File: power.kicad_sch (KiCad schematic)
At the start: 23 parts, among them J1 Power, Q1 SI2301CDS-T1-GE3, U1 TMA-1212D, U2 TPS54302

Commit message: add placement notes into the schematic
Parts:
- U1: Placement (none) -> Separate from analog signal path. Digital ground side.
- U2: Placement (none) -> Follow TPS54302 datasheet layout rules. Digital ground. Kee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
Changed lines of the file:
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@@
+			)
+		)
+		(property "Placement" "Follow TPS54302 datasheet layout rules. Digital ground. Keep switching noise away from analog section."
+			(at 161.29 52.07 0)
+			(effects
+				(font
+					(size 1.27 1.27)
+				)
+				(hide yes)
 			)
 		)
@@
 			(at 60.96 130.81 0)
 			(effects
+				(font
+					(size 1.27 1.27)
+				)
+				(hide yes)
+			)
+		)
+		(property "Placement" "Separate from analog signal path. Digital ground side."
+			(at 60.96 130.81 0)
+			(effects

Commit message: dealing with protection circuit changes
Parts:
- added D2: 1N4733A, Diode_THT:D_DO-41_SOD81_P10.16mm_Horizontal, symbol Device:D_Zener
- renumbered C5 to C4, C4 to C5
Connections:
- net +5V: now also D2.2 (A)
- net GND: now also D2.1 (K)

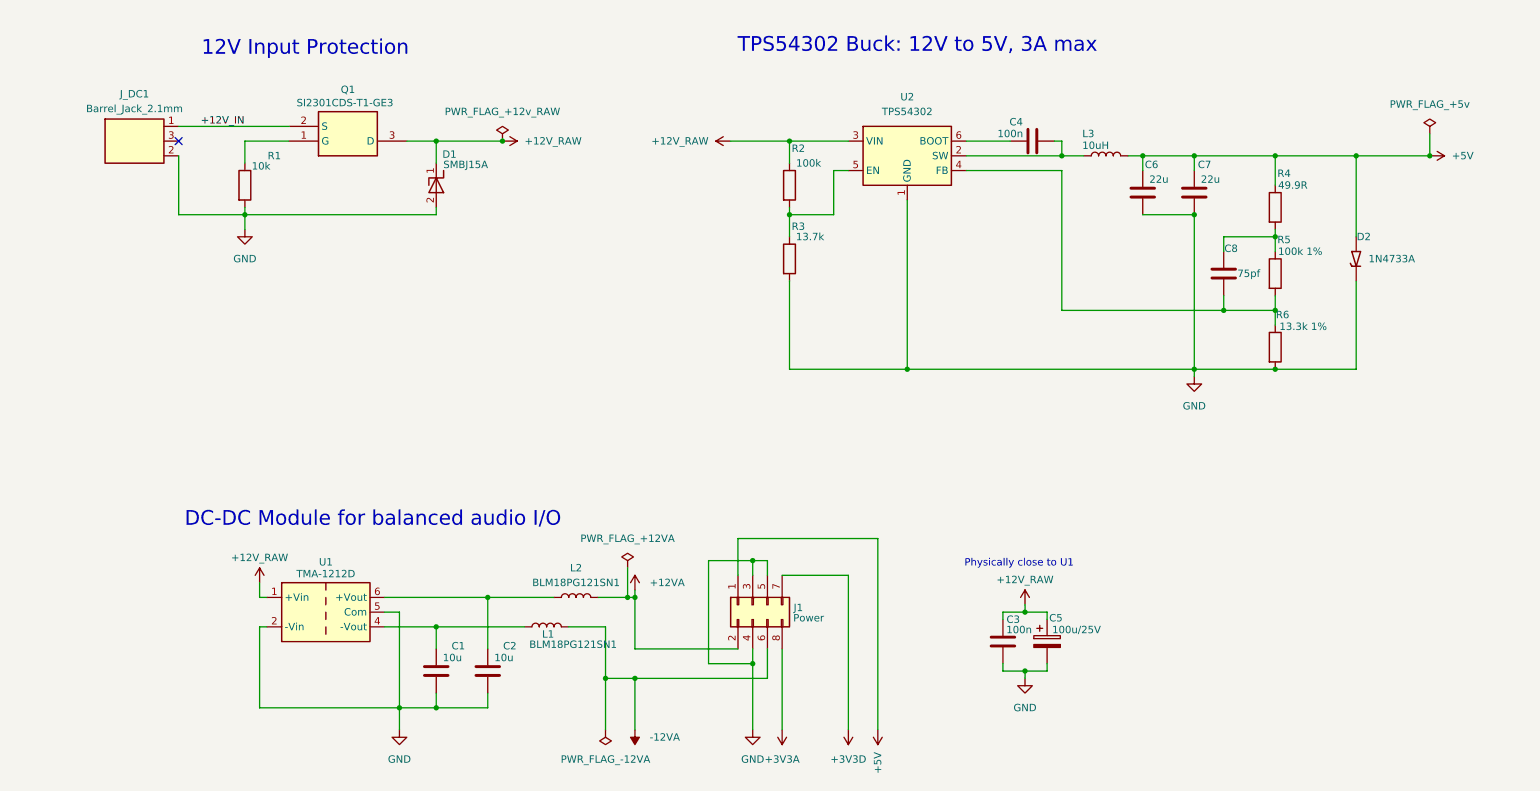
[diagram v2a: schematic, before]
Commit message: audio input for rev 2 laid out in schematic
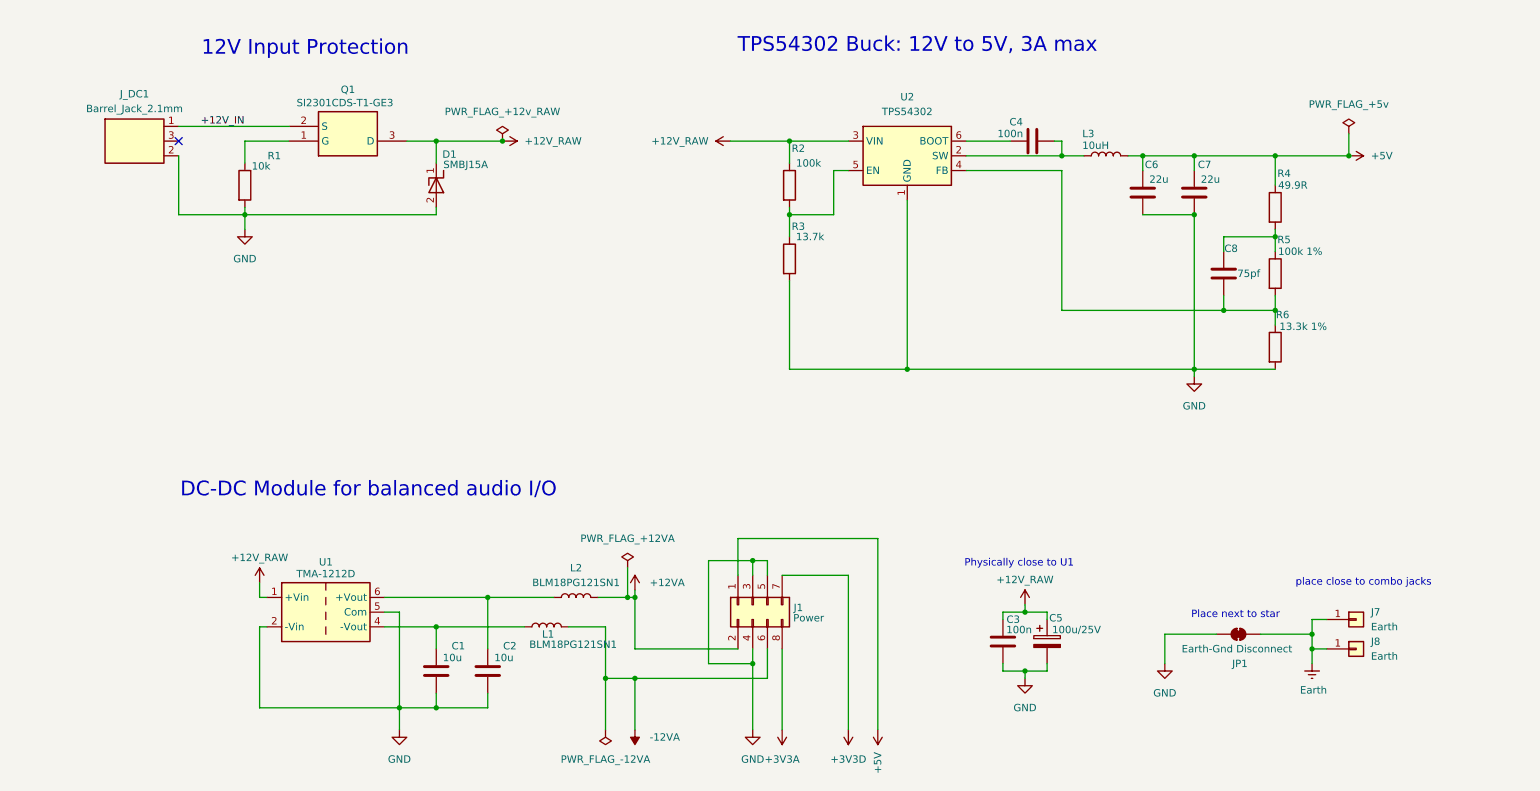
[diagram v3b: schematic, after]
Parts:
- removed D2: 1N4733A, Diode_THT:D_DO-41_SOD81_P10.16mm_Horizontal, symbol Device:D_Zener
- added J7, J8: Earth, MountingHole:MountingHole_3.2mm_M3_Pad_Via, symbol Connector_Generic:Conn_01x01
- added JP1: Earth-Gnd Disconnect, Jumper:SolderJumper-2_P1.3mm_Bridged_Pad1.0x1.5mm, symbol Jumper:SolderJumper_2_Bridged
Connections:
- net GND: now also JP1.1 (A)
- new net Earth: J7.1 (Pin_1), J8.1 (Pin_1), JP1.2 (B)
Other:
- note added: "Place next to star"
- note added: "place close to combo jacks"
- title: Triptech - Power Supply -> Daisy-Studio

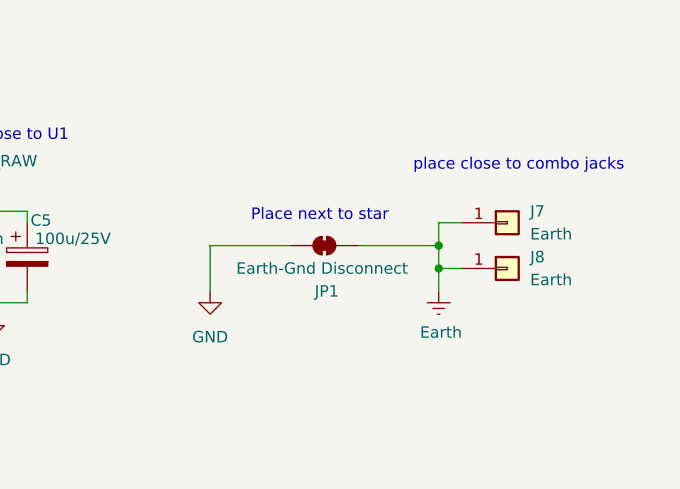
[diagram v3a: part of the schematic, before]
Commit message: Cleanup and review of input pt 1
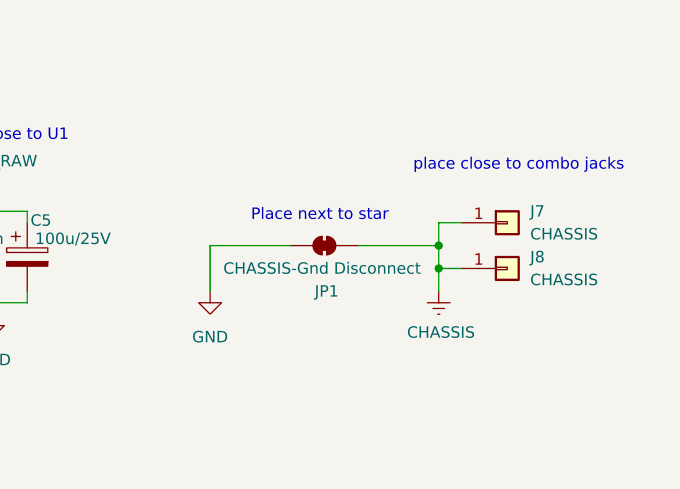
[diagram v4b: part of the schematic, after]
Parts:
- J7, J8: value Earth -> CHASSIS
- JP1: value Earth-Gnd Disconnect -> CHASSIS-Gnd Disconnect
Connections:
- net Earth renamed CHASSIS
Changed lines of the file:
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@@
 			)
 		)
-		(property "Value" "Earth"
+		(property "Value" "CHASSIS"
 			(at 241.3 133.3499 0)
 			(effects
@@
 			)
 		)
-		(property "Value" "Earth-Gnd Disconnect"
+		(property "Value" "CHASSIS-Gnd Disconnect"
 			(at 218.186 137.16 0)
 			(effects
@@
 			)
 		)
-		(property "Value" "Earth"
+		(property "Value" "CHASSIS"
 			(at 231.394 144.272 0)
 			(effects
@@
 			)
 		)
-		(property "Value" "Earth"
+		(property "Value" "CHASSIS"
 			(at 241.3 138.4299 0)
 			(effects

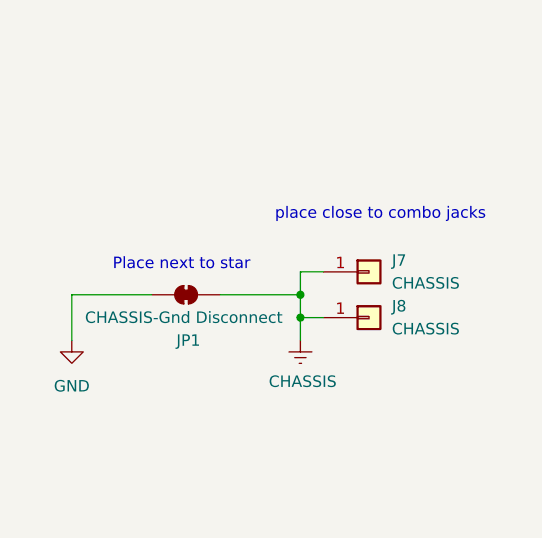
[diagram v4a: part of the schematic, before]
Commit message: fix some footprints
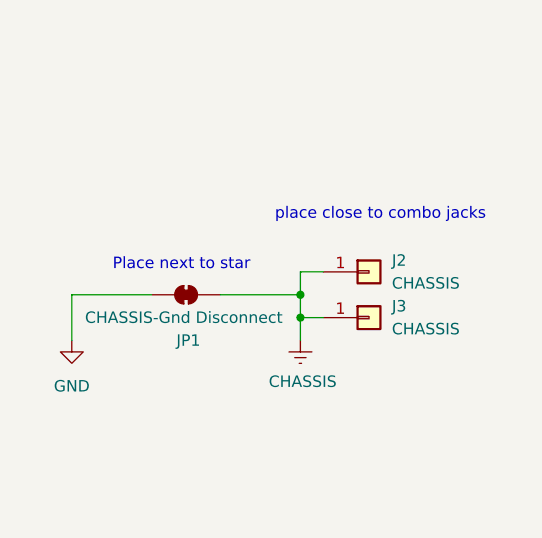
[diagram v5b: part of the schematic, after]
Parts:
- renumbered J7 to J2, J8 to J3
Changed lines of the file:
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@@
 		(dnp no)
 		(fields_autoplaced yes)
-		(property "Reference" "#PWR062"
+		(property "Reference" "#PWR014"
 			(at 205.74 146.05 0)
 			(effects
@@
 			(project "daisy-studio"
 				(path "/55cca6a8-30da-4c13-b2f2-a01401e2b54c/a1b2c3d4-1111-4000-8000-000000000001"
-					(reference "#PWR062")
+					(reference "#PWR014")
 					(unit 1)
 				)
@@
 		(dnp no)
 		(fields_autoplaced yes)
-		(property "Reference" "J7"
+		(property "Reference" "J2"
 			(at 241.3 130.8099 0)
 			(effects
@@
 			(project "daisy-studio"
 				(path "/55cca6a8-30da-4c13-b2f2-a01401e2b54c/a1b2c3d4-1111-4000-8000-000000000001"
-					(reference "J7")
+					(reference "J2")
 					(unit 1)
 				)
@@
 		(on_board yes)
 		(dnp no)
-		(property "Reference" "#PWR063"
+		(property "Reference" "#PWR016"
 			(at 231.14 146.05 0)
 			(effects
@@
 			(project "daisy-studio"
 				(path "/55cca6a8-30da-4c13-b2f2-a01401e2b54c/a1b2c3d4-1111-4000-8000-000000000001"
-					(reference "#PWR063")
+					(reference "#PWR016")
 					(unit 1)
 				)
@@
 		(dnp no)
 		(fields_autoplaced yes)
-		(property "Reference" "#PWR014"
+		(property "Reference" "#PWR015"
 			(at 210.82 96.52 0)
 			(effects
@@
 			(project "triptech"
 				(path "/55cca6a8-30da-4c13-b2f2-a01401e2b54c/a1b2c3d4-1111-4000-8000-000000000001"
-					(reference "#PWR014")
+					(reference "#PWR015")
 					(unit 1)
 				)
@@
 		(dnp no)
 		(fields_autoplaced yes)
-		(property "Reference" "J8"
+		(property "Reference" "J3"
 			(at 241.3 135.8899 0)
 			(effects
@@
 			(project "daisy-studio"
 				(path "/55cca6a8-30da-4c13-b2f2-a01401e2b54c/a1b2c3d4-1111-4000-8000-000000000001"
-					(reference "J8")
+					(reference "J3")
 					(unit 1)
 				)
@@
 		(dnp no)
 		(fields_autoplaced yes)
-		(property "Reference" "#PWR015"
+		(property "Reference" "#PWR017"
 			(at 233.68 52.07 0)
 			(effects
@@
 			(project ""
 				(path "/55cca6a8-30da-4c13-b2f2-a01401e2b54c/a1b2c3d4-1111-4000-8000-000000000001"
-					(reference "#PWR015")
-					(unit 1)
-				)
+					(reference "#PWR017")
+					(unit 1)
+				)

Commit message: starting on output
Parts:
- C1, C2: value 10u -> C
- C3, C4: value 100n -> C
- C5: value 100u/25V -> C_Polarized
- C6, C7: value 22u -> C
- C8: value 75pf -> C
- D1: value SMBJ15A -> D_TVS
- H2: renamed from J2; value CHASSIS -> MountingHole_Pad; symbol Connector_Generic:Conn_01x01 -> Mechanical:MountingHole_Pad; now left out of the parts list
- H3: renamed from J3; value CHASSIS -> MountingHole_Pad; symbol Connector_Generic:Conn_01x01 -> Mechanical:MountingHole_Pad; now left out of the parts list
- IC1: renamed from Q1; footprint Package_TO_SOT_SMD:SOT-23 -> daisy-studio:SOT95P237X112-3N
- J1: value Power -> Conn_02x04_Odd_Even
- J1: renamed from J_DC1; value Barrel_Jack_2.1mm -> Barrel_Jack_MountingPin
- JP1: value CHASSIS-Gnd Disconnect -> SolderJumper_2_Bridged
- L1, L2: value BLM18PG121SN1 -> L
- L3: value 10uH -> L
- R1: value 10k -> R
- R2: value 100k -> R
- R3: value 13.7k -> R
- R4: value 49.9R -> R
- R5: value 100k 1% -> R
- R6: value 13.3k 1% -> R
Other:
- moved on the sheet: C3, C5

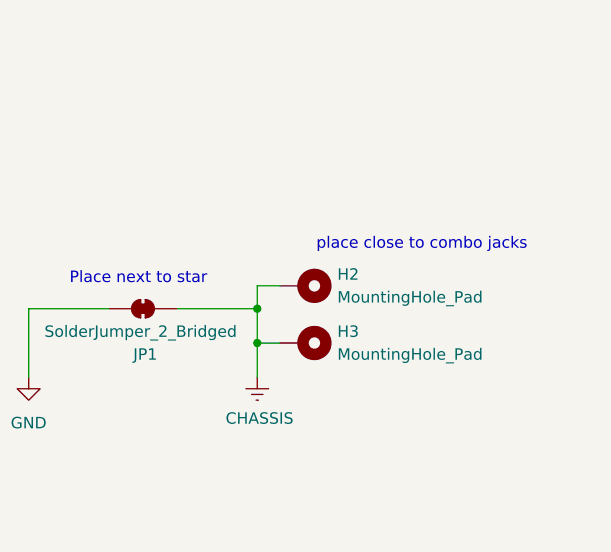
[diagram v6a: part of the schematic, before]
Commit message: daughterboard added
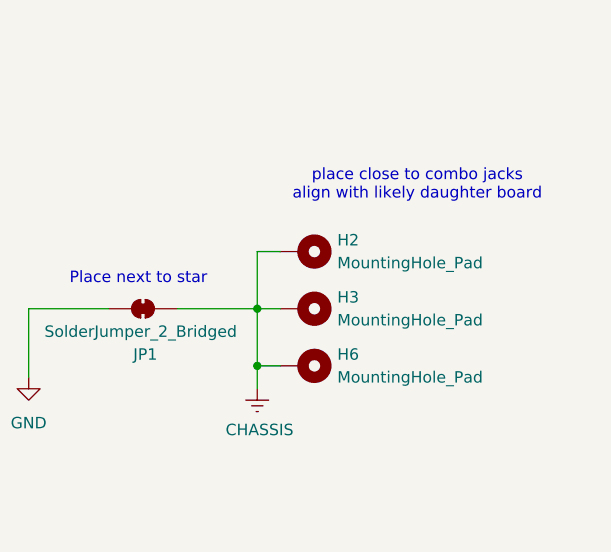
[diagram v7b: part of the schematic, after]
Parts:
- added H6: MountingHole_Pad, MountingHole:MountingHole_3.2mm_M3_Pad_Via, symbol Mechanical:MountingHole_Pad
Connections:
- net CHASSIS: now also H6.1
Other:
- note added: "place close to combo jacks align with likely daughter board"
- note removed: "place close to combo jacks"
- moved on the sheet: H2, H3
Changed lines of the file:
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@@
 		)
 	)
-	(text "place close to combo jacks\n"
+	(text "place close to combo jacks\nalign with likely daughter board\n"
 		(exclude_from_sim no)
-		(at 249.428 127.508 0)
+		(at 248.92 120.904 0)
 		(effects
 			(font
@@
 	)
 	(junction
-		(at 114.3 128.27)
+		(at 231.14 140.97)
 		(diameter 0)
 		(color 0 0 0 0)
 	)
 	(junction
-		(at 231.14 138.43)
+		(at 114.3 128.27)
 		(diameter 0)
 		(color 0 0 0 0)
@@
 	(wire
 		(pts
-			(xy 231.14 132.08) (xy 233.68 132.08)
+			(xy 231.14 128.27) (xy 233.68 128.27)
 		)
 		(stroke
@@
 	(wire
 		(pts
+			(xy 231.14 128.27) (xy 231.14 134.62)
+		)
+		(stroke
+			(width 0)
+			(type default)
+		)
+	)
+	(wire
+		(pts
 			(xy 134.62 139.7) (xy 134.62 151.13)
 		)
@@
 	(wire
 		(pts
-			(xy 46.99 64.77) (xy 46.99 62.23)
+			(xy 231.14 134.62) (xy 231.14 140.97)
 		)
 		(stroke
@@
 	(wire
 		(pts
-			(xy 71.12 130.81) (xy 73.66 130.81)
+			(xy 46.99 64.77) (xy 46.99 62.23)
 		)
 		(stroke
@@
 	(wire
 		(pts
-			(xy 201.93 62.23) (xy 210.82 62.23)
+			(xy 71.12 130.81) (xy 73.66 130.81)
 		)
 		(stroke
@@
 	(wire
 		(pts
-			(xy 231.14 138.43) (xy 231.14 142.24)
+			(xy 201.93 62.23) (xy 210.82 62.23)
 		)
 		(stroke
@@
 	(wire
 		(pts
-			(xy 231.14 134.62) (xy 231.14 138.43)
-		)
-		(stroke
-			(width 0)
-			(type default)
-		)
-	)
-	(wire
-		(pts
 			(xy 187.96 49.53) (xy 187.96 52.07)
 		)
@@
 	(wire
 		(pts
+			(xy 231.14 140.97) (xy 233.68 140.97)
+		)
+		(stroke
+			(width 0)
+			(type default)
+		)
+	)
+	(wire
+		(pts
 			(xy 139.7 137.16) (xy 139.7 151.13)
 		)
@@
 	(wire
 		(pts
-			(xy 231.14 138.43) (xy 233.68 138.43)
+			(xy 231.14 134.62) (xy 233.68 134.62)
 		)
 		(stroke
@@
 	(wire
 		(pts
-			(xy 231.14 132.08) (xy 231.14 134.62)
+			(xy 187.96 49.53) (xy 186.69 49.53)
 		)
 		(stroke
@@
 	(wire
 		(pts
-			(xy 187.96 49.53) (xy 186.69 49.53)
+			(xy 210.82 90.17) (xy 210.82 88.9)
 		)
 		(stroke
@@
 	(wire
 		(pts
-			(xy 210.82 90.17) (xy 210.82 88.9)
+			(xy 46.99 49.53) (xy 54.61 49.53)
 		)
 		(stroke
@@
 	(wire
 		(pts
-			(xy 46.99 49.53) (xy 54.61 49.53)
+			(xy 184.15 129.54) (xy 184.15 133.35)
 		)
 		(stroke
@@
 	(wire
 		(pts
-			(xy 184.15 129.54) (xy 184.15 133.35)
+			(xy 140.97 62.23) (xy 140.97 60.96)
 		)
 		(stroke
@@
 	(wire
 		(pts
-			(xy 140.97 62.23) (xy 140.97 60.96)
+			(xy 46.99 62.23) (xy 80.01 62.23)
 		)
 		(stroke
@@
 	(wire
 		(pts
-			(xy 46.99 62.23) (xy 80.01 62.23)
+			(xy 80.01 60.96) (xy 80.01 62.23)
 		)
 		(stroke
@@
 	(wire
 		(pts
-			(xy 80.01 60.96) (xy 80.01 62.23)
+			(xy 231.14 140.97) (xy 231.14 143.51)
 		)
 		(stroke
@@
 	(symbol
 		(lib_id "Mechanical:MountingHole_Pad")
-		(at 236.22 132.08 270)
+		(at 236.22 128.27 270)
 		(unit 1)
 		(exclude_from_sim no)
@@
 		(fields_autoplaced yes)
 		(property "Reference" "H2"
-			(at 240.03 130.8099 90)
+			(at 240.03 126.9999 90)
 			(effects
 				(font
@@
 		)
 		(property "Value" "MountingHole_Pad"
-			(at 240.03 133.3499 90)
+			(at 240.03 129.5399 90)
 			(effects
 				(font
@@
 		)
 		(property "Footprint" "MountingHole:MountingHole_3.2mm_M3_Pad_Via"
-			(at 236.22 132.08 0)
+			(at 236.22 128.27 0)
 			(effects
 				(font
@@
 		)
 		(property "Datasheet" "~"
-			(at 236.22 132.08 0)
+			(at 236.22 128.27 0)
 			(effects
 				(font
@@
 		)
 		(property "Description" "Mounting Hole with connection"
-			(at 236.22 132.08 0)
+			(at 236.22 128.27 0)
 			(effects
 				(font
@@
 	(symbol
 		(lib_id "power:Earth")
-		(at 231.14 142.24 0)
+		(at 231.14 143.51 0)
 		(unit 1)
 		(exclude_from_sim no)
@@
 		(dnp no)
 		(property "Reference" "#PWR16"
-			(at 231.14 148.59 0)
+			(at 231.14 149.86 0)
 			(effects
 				(font
@@
 		)
 		(property "Value" "CHASSIS"
-			(at 231.394 146.812 0)
+			(at 231.394 148.082 0)
 			(effects
 				(font
@@
 		)
 		(property "Footprint" ""
-			(at 231.14 142.24 0)
+			(at 231.14 143.51 0)
 			(effects
 				(font
@@
 		)
 		(property "Datasheet" "~"
-			(at 231.14 142.24 0)
+			(at 231.14 143.51 0)
 			(effects
 				(font
@@
 		)
 		(property "Description" "Power symbol creates a global label with name \"Earth\""
-			(at 231.14 142.24 0)
+			(at 231.14 143.51 0)
 			(effects
 				(font
@@
 	)
 	(symbol
+		(lib_id "Mechanical:MountingHole_Pad")
+		(at 236.22 140.97 270)
+		(unit 1)
+		(exclude_from_sim no)
+		(in_bom no)
+		(on_board yes)
+		(dnp no)
+		(fields_autoplaced yes)
+		(property "Reference" "H6"
+			(at 240.03 139.6999 90)
+			(effects
+				(font
+					(size 1.27 1.27)
+				)
+				(justify left)
+			)
+		)
+		(property "Value" "MountingHole_Pad"
+			(at 240.03 142.2399 90)
+			(effects
+				(font
+					(size 1.27 1.27)
+				)
+				(justify left)
+			)
+		)
+		(property "Footprint" "MountingHole:MountingHole_3.2mm_M3_Pad_Via"
+			(at 236.22 140.97 0)
+			(effects
+				(font
+					(size 1.27 1.27)
+				)
+				(hide yes)
+			)
+		)
+		(property "Datasheet" "~"
+			(at 236.22 140.97 0)
+			(effects
+				(font
+					(size 1.27 1.27)
+				)
+				(hide yes)
+			)
+		)
+		(property "Description" "Mounting Hole with connection"
+			(at 236.22 140.97 0)
+			(effects
+				(font
+					(size 1.27 1.27)
+				)
+				(hide yes)
+			)
+		)
+		(pin "1"
+		)
+		(instances
+			(project "daisy-studio"
+				(path "/55cca6a8-30da-4c13-b2f2-a01401e2b54c/a1b2c3d4-1111-4000-8000-000000000001"
+					(reference "H6")
+					(unit 1)
+				)
+			)
+		)
+	)
+	(symbol
 		(lib_id "power:GND")
 		(at 210.82 90.17 0)
@@
 	(symbol
 		(lib_id "Mechanical:MountingHole_Pad")
-		(at 236.22 138.43 270)
+		(at 236.22 134.62 270)
 		(unit 1)
 		(exclude_from_sim no)
@@
 		(fields_autoplaced yes)
 		(property "Reference" "H3"
-			(at 240.03 137.1599 90)
+			(at 240.03 133.3499 90)
 			(effects
 				(font
@@
 		)
 		(property "Value" "MountingHole_Pad"
-			(at 240.03 139.6999 90)
+			(at 240.03 135.8899 90)
 			(effects
 				(font
@@
 		)
 		(property "Footprint" "MountingHole:MountingHole_3.2mm_M3_Pad_Via"
-			(at 236.22 138.43 0)
+			(at 236.22 134.62 0)
 			(effects
 				(font
@@
 		)
 		(property "Datasheet" "~"
-			(at 236.22 138.43 0)
+			(at 236.22 134.62 0)
 			(effects
 				(font
@@
 		)
 		(property "Description" "Mounting Hole with connection"
-			(at 236.22 138.43 0)
+			(at 236.22 134.62 0)
 			(effects
 				(font
